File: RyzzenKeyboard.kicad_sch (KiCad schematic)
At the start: 30 parts, among them IC1 LD39100PU33RY, J1 TC2050, J2 Conn_01x16_Socket, J3 Conn_01x16_Socket, J4 USB_C_Receptacle_USB2.0_14P, U1 STM32F411CEUx, U37 W25Q32JVSS, Y1 25MHz

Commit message: [FIX](General) footprints
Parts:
- IC1: footprint SON95P300X300X90-7N-D -> LD39100PU33RY:SON95P300X300X90-7N-D
- renumbered D37 to D1, D1 to D2, J2 to J1, J3 to J2, J1 to J3, R4 to R1, R1 to R2, R11 to R3, R10 to R4, R2 to R5, R3 to R6, U37 to U1, U1 to U2
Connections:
- net VBUS: now also D1.2 (A); no longer D1.1 (K)
- net nCS0: no longer J1.8 (Pin_8), J2.8 (Pin_8)
- net nCS1: no longer J1.7 (Pin_7), J2.7 (Pin_7)
- net nCS2: now also J1.8 (Pin_8)
- net nCS3: now also J1.7 (Pin_7)
- net nCS4: now also J2.8 (Pin_8)
- net nCS5: now also J2.7 (Pin_7)
- net at J4.A4 (VBUS), J4.A9 (VBUS), J4.B4 (VBUS)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: now also D1.1 (K); no longer D1.2 (A)
- net Din renamed LED_Din
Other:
- sheet LEDs ports: added LED_5V, LED_DATA, LED_GND; removed Din, GND, Vcc
- moved on the sheet: D1

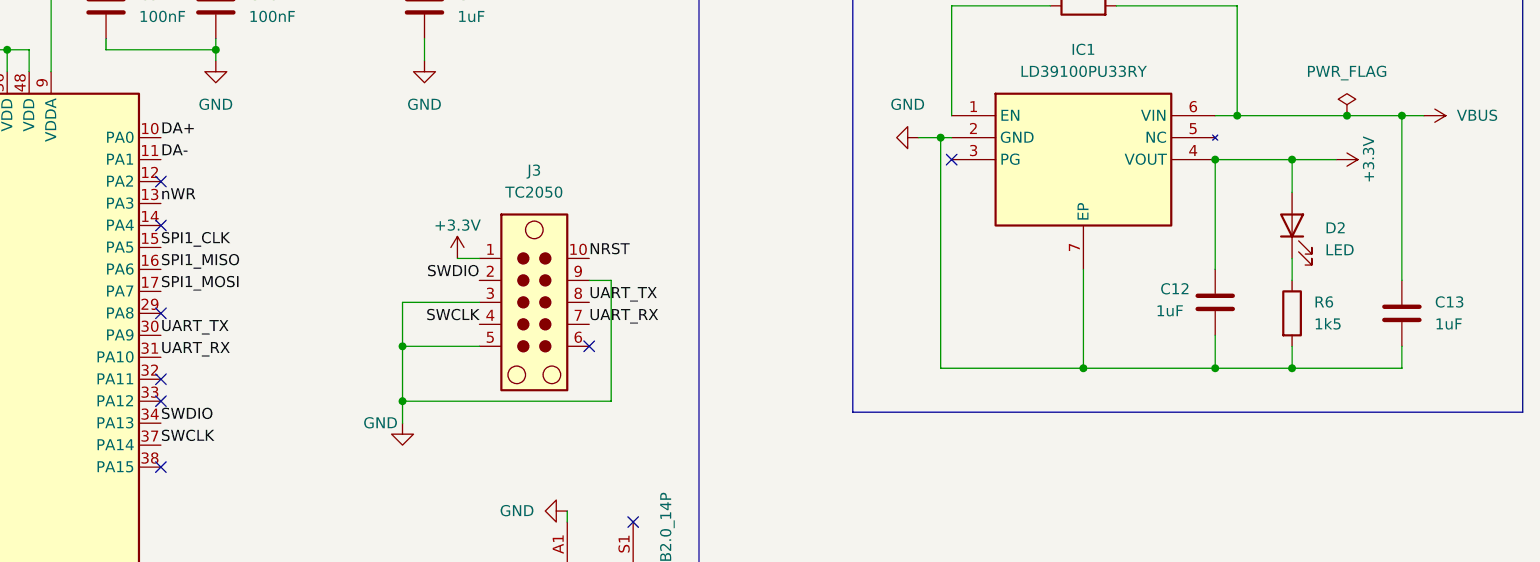
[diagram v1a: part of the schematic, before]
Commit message: [FIX](USB) main usb net labels
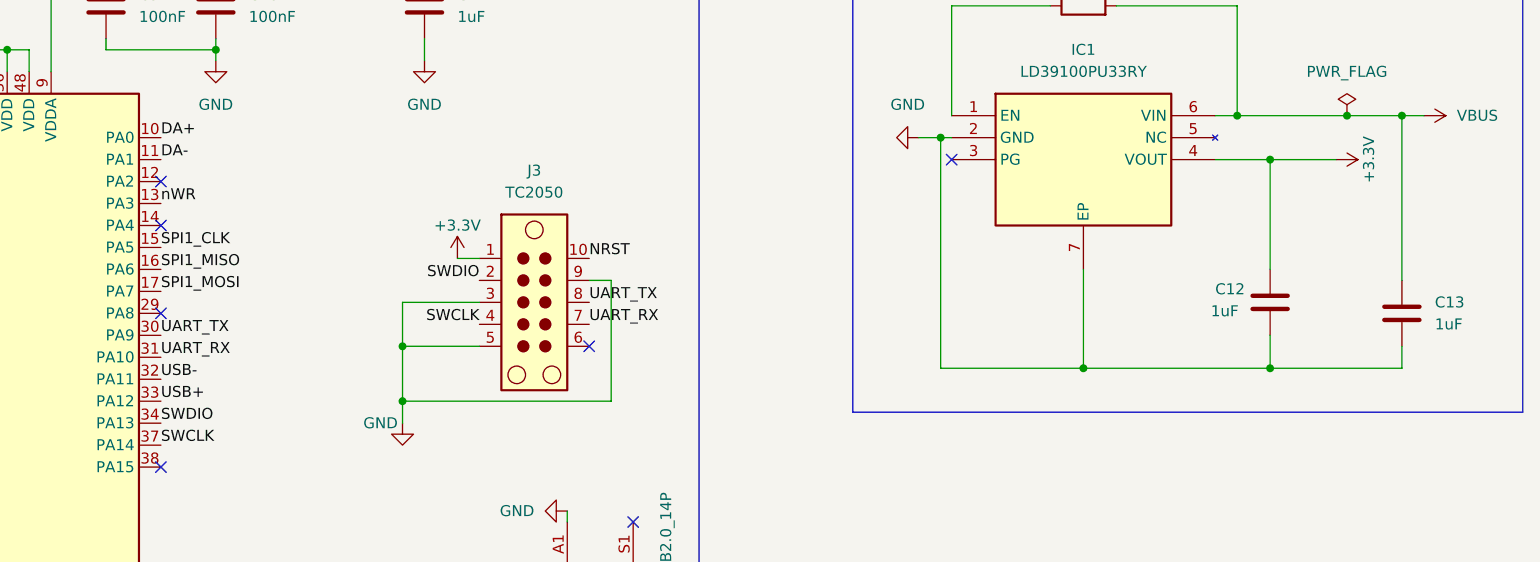
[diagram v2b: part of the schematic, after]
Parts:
- removed D2: LED, symbol Device:LED
- removed R6: 1k5, symbol Device:R
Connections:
- net USB+: now also U2.33 (PA12)
- net USB-: now also U2.32 (PA11)
- no-connect marks 13 -> 11
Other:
- moved on the sheet: C12
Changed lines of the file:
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@@
 	)
 	(junction
-		(at 247.65 80.01)
-		(diameter 0)
-		(color 0 0 0 0)
-	)
-	(junction
 		(at 35.56 43.18)
 		(diameter 0)
@@
 	)
 	(junction
-		(at 44.45 34.29)
+		(at 245.11 80.01)
 		(diameter 0)
 		(color 0 0 0 0)
 	)
 	(junction
-		(at 247.65 55.88)
+		(at 44.45 34.29)
 		(diameter 0)
 		(color 0 0 0 0)
@@
 	)
 	(junction
-		(at 238.76 80.01)
-		(diameter 0)
-		(color 0 0 0 0)
-	)
-	(junction
 		(at 58.42 91.44)
 		(diameter 0)
@@
 	)
 	(junction
-		(at 238.76 55.88)
+		(at 96.52 43.18)
 		(diameter 0)
 		(color 0 0 0 0)
 	)
 	(junction
-		(at 96.52 43.18)
+		(at 99.06 43.18)
 		(diameter 0)
 		(color 0 0 0 0)
 	)
 	(junction
-		(at 99.06 43.18)
+		(at 104.14 34.29)
 		(diameter 0)
 		(color 0 0 0 0)
 	)
 	(junction
-		(at 104.14 34.29)
+		(at 245.11 55.88)
 		(diameter 0)
 		(color 0 0 0 0)
@@
 	)
 	(no_connect
-		(at 116.84 83.82)
-	)
-	(no_connect
-		(at 116.84 81.28)
-	)
-	(no_connect
 		(at 166.37 77.47)
 	)
@@
 	(wire
 		(pts
-			(xy 223.52 80.01) (xy 238.76 80.01)
+			(xy 223.52 80.01) (xy 245.11 80.01)
 		)
 		(stroke
@@
 	(wire
 		(pts
-			(xy 247.65 55.88) (xy 252.73 55.88)
-		)
-		(stroke
-			(width 0)
-			(type default)
-		)
-	)
-	(wire
-		(pts
 			(xy 147.32 115.57) (xy 148.59 115.57)
 		)
@@
 	(wire
 		(pts
-			(xy 247.65 80.01) (xy 260.35 80.01)
+			(xy 62.23 76.2) (xy 62.23 83.82)
 		)
 		(stroke
@@
 	(wire
 		(pts
-			(xy 62.23 76.2) (xy 62.23 83.82)
+			(xy 110.49 34.29) (xy 116.84 34.29)
 		)
 		(stroke
@@
 	(wire
 		(pts
-			(xy 110.49 34.29) (xy 116.84 34.29)
+			(xy 147.32 30.48) (xy 147.32 34.29)
 		)
 		(stroke
@@
 	(wire
 		(pts
-			(xy 147.32 30.48) (xy 147.32 34.29)
+			(xy 101.6 43.18) (xy 101.6 45.72)
 		)
 		(stroke
@@
 	(wire
 		(pts
-			(xy 101.6 43.18) (xy 101.6 45.72)
+			(xy 31.75 123.19) (xy 27.94 123.19)
 		)
 		(stroke
@@
 	(wire
 		(pts
-			(xy 31.75 123.19) (xy 27.94 123.19)
+			(xy 245.11 80.01) (xy 260.35 80.01)
 		)
 		(stroke
@@
 	(wire
 		(pts
-			(xy 247.65 67.31) (xy 247.65 69.85)
-		)
-		(stroke
-			(width 0)
-			(type default)
-		)
-	)
-	(wire
-		(pts
 			(xy 148.59 123.19) (xy 147.32 123.19)
 		)
@@
 	(wire
 		(pts
-			(xy 238.76 80.01) (xy 247.65 80.01)
-		)
-		(stroke
-			(width 0)
-			(type default)
-		)
-	)
-	(wire
-		(pts
 			(xy 104.14 34.29) (xy 110.49 34.29)
 		)
@@
 	(wire
 		(pts
+			(xy 245.11 55.88) (xy 252.73 55.88)
+		)
+		(stroke
+			(width 0)
+			(type default)
+		)
+	)
+	(wire
+		(pts
 			(xy 146.05 120.65) (xy 147.32 120.65)
 		)
@@
 	(wire
 		(pts
-			(xy 238.76 68.58) (xy 238.76 55.88)
+			(xy 245.11 68.58) (xy 245.11 55.88)
 		)
 		(stroke
@@
 	(wire
 		(pts
-			(xy 247.65 55.88) (xy 247.65 59.69)
-		)
-		(stroke
-			(width 0)
-			(type default)
-		)
-	)
-	(wire
-		(pts
 			(xy 58.42 91.44) (xy 62.23 91.44)
 		)
@@
 	(wire
 		(pts
-			(xy 238.76 55.88) (xy 247.65 55.88)
-		)
-		(stroke
-			(width 0)
-			(type default)
-		)
-	)
-	(wire
-		(pts
-			(xy 247.65 77.47) (xy 247.65 80.01)
+			(xy 238.76 55.88) (xy 245.11 55.88)
 		)
 		(stroke
@@
 	(wire
 		(pts
-			(xy 238.76 76.2) (xy 238.76 80.01)
+			(xy 245.11 76.2) (xy 245.11 80.01)
 		)
 		(stroke
@@
 		)
 	)
+	(label "USB+"
+		(at 116.84 83.82 0)
+		(effects
+			(font
+				(size 1.27 1.27)
+			)
+			(justify left bottom)
+		)
+	)
 	(label "A3"
 		(at 81.28 106.68 180)
@@
 		)
 	)
+	(label "USB-"
+		(at 116.84 81.28 0)
+		(effects
+			(font
+				(size 1.27 1.27)
+			)
+			(justify left bottom)
+		)
+	)
 	(label "SPI1_MISO"
 		(at 116.84 68.58 0)
@@
 	(symbol
 		(lib_id "Device:C")
-		(at 238.76 72.39 0)
+		(at 245.11 72.39 0)
 		(unit 1)
 		(exclude_from_sim no)
@@
 		(dnp no)
 		(property "Reference" "C12"
-			(at 232.41 70.866 0)
+			(at 238.76 70.866 0)
 			(effects
 				(font
@@
 		)
 		(property "Value" "1uF"
-			(at 231.902 73.406 0)
+			(at 238.252 73.406 0)
 			(effects
 				(font
@@
 		)
 		(property "Footprint" ""
-			(at 239.7252 76.2 0)
+			(at 246.0752 76.2 0)
 			(effects
 				(font
@@
 		)
 		(property "Datasheet" "~"
-			(at 238.76 72.39 0)
+			(at 245.11 72.39 0)
 			(effects
 				(font
@@
 		)
 		(property "Description" "Unpolarized capacitor"
-			(at 238.76 72.39 0)
+			(at 245.11 72.39 0)
 			(effects
 				(font
@@
 	)
 	(symbol
-		(lib_id "Device:R")
-		(at 247.65 73.66 0)
-		(unit 1)
-		(exclude_from_sim no)
-		(in_bom yes)
-		(on_board yes)
-		(dnp no)
-		(fields_autoplaced yes)
-		(property "Reference" "R6"
-			(at 250.19 72.3899 0)
-			(effects
-				(font
-					(size 1.27 1.27)
-				)
-				(justify left)
-			)
-		)
-		(property "Value" "1k5"
-			(at 250.19 74.9299 0)
-			(effects
-				(font
-					(size 1.27 1.27)
-				)
-				(justify left)
-			)
-		)
-		(property "Footprint" ""
-			(at 245.872 73.66 90)
-			(effects
-				(font
-					(size 1.27 1.27)
-				)
-				(hide yes)
-			)
-		)
-		(property "Datasheet" "~"
-			(at 247.65 73.66 0)
-			(effects
-				(font
-					(size 1.27 1.27)
-				)
-				(hide yes)
-			)
-		)
-		(property "Description" "Resistor"
-			(at 247.65 73.66 0)
-			(effects
-				(font
-					(size 1.27 1.27)
-				)
-				(hide yes)
-			)
-		)
-		(pin "2"
-		)
-		(pin "1"
-		)
-		(instances
-			(project "RyzzenKeyboard"
-				(path "/5d44d704-6136-40a8-98a4-93f001ea8743"
-					(reference "R6")
-					(unit 1)
-				)
-			)
-		)
-	)
-	(symbol
 		(lib_id "power:GND")
 		(at 130.81 156.21 90)
@@
 	)
 	(symbol
-		(lib_id "Device:LED")
-		(at 247.65 63.5 90)
-		(unit 1)
-		(exclude_from_sim no)
-		(in_bom yes)
-		(on_board yes)
-		(dnp no)
-		(fields_autoplaced yes)
-		(property "Reference" "D2"
-			(at 251.46 63.8174 90)
-			(effects
-				(font
-					(size 1.27 1.27)
-				)
-				(justify right)
-			)
-		)
-		(property "Value" "LED"
-			(at 251.46 66.3574 90)
-			(effects
-				(font
-					(size 1.27 1.27)
-				)
-				(justify right)
-			)
-		)
-		(property "Footprint" ""
-			(at 247.65 63.5 0)
-			(effects
-				(font
-					(size 1.27 1.27)
-				)
-				(hide yes)
-			)
-		)
-		(property "Datasheet" "~"
-			(at 247.65 63.5 0)
-			(effects
-				(font
-					(size 1.27 1.27)
-				)
-				(hide yes)
-			)
-		)
-		(property "Description" "Light emitting diode"
-			(at 247.65 63.5 0)
-			(effects
-				(font
-					(size 1.27 1.27)
-				)
-				(hide yes)
-			)
-		)
-		(property "Sim.Pins" "1=K 2=A"
-			(at 247.65 63.5 0)
-			(effects
-				(font
-					(size 1.27 1.27)
-				)
-				(hide yes)
-			)
-		)
-		(pin "2"
-		)
-		(pin "1"
-		)
-		(instances
-			(project "RyzzenKeyboard"
-				(path "/5d44d704-6136-40a8-98a4-93f001ea8743"
-					(reference "D2")
-					(unit 1)
-				)
-			)
-		)
-	)
-	(symbol
 		(lib_id "Memory_Flash:W25Q32JVSS")
 		(at 41.91 120.65 0)
@@
 			(project "RyzzenKeyboard"
 				(path "/5d44d704-6136-40a8-98a4-93f001ea8743"
-					(page "106")
+					(page "120")
 				)
 			)
@@
 			(project "RyzzenKeyboard"
 				(path "/5d44d704-6136-40a8-98a4-93f001ea8743"
-					(page "108")
+					(page "5")
 				)
 			)

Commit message: [ADD](General) added all footprints expect leds
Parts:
- C1, C10, C11, C12, C13, C2, C3, C4, C5, C6, C7, C8, C9: footprint (none) -> Capacitor_SMD:C_0603_1608Metric_Pad1.08x0.95mm_HandSolder
- J1, J2: footprint (none) -> Connector_JST:JST_XH_S16B-XH-A_1x16_P2.50mm_Horizontal
- R1, R2, R3, R4, R5: footprint (none) -> Resistor_SMD:R_0603_1608Metric_Pad0.98x0.95mm_HandSolder
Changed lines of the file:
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@@
 			)
 		)
-		(property "Footprint" ""
+		(property "Footprint" "Capacitor_SMD:C_0603_1608Metric_Pad1.08x0.95mm_HandSolder"
 			(at 49.53 54.3052 0)
 			(effects
@@
 			)
 		)
-		(property "Footprint" ""
+		(property "Footprint" "Resistor_SMD:R_0603_1608Metric_Pad0.98x0.95mm_HandSolder"
 			(at 223.52 39.878 90)
 			(effects
@@
 			)
 		)
-		(property "Footprint" ""
+		(property "Footprint" "Capacitor_SMD:C_0603_1608Metric_Pad1.08x0.95mm_HandSolder"
 			(at 58.1152 41.91 0)
 			(effects
@@
 			)
 		)
-		(property "Footprint" ""
+		(property "Footprint" "Capacitor_SMD:C_0603_1608Metric_Pad1.08x0.95mm_HandSolder"
 			(at 111.4552 41.91 0)
 			(effects
@@
 			)
 		)
-		(property "Footprint" ""
+		(property "Footprint" "Capacitor_SMD:C_0603_1608Metric_Pad1.08x0.95mm_HandSolder"
 			(at 32.7152 41.91 0)
 			(effects
@@
 			)
 		)
-		(property "Footprint" ""
+		(property "Footprint" "Capacitor_SMD:C_0603_1608Metric_Pad1.08x0.95mm_HandSolder"
 			(at 47.9552 91.44 0)
 			(effects
@@
 			)
 		)
-		(property "Footprint" ""
+		(property "Footprint" "Capacitor_SMD:C_0603_1608Metric_Pad1.08x0.95mm_HandSolder"
 			(at 70.8152 41.91 0)
 			(effects
@@
 			)
 		)
-		(property "Footprint" ""
+		(property "Footprint" "Capacitor_SMD:C_0603_1608Metric_Pad1.08x0.95mm_HandSolder"
 			(at 246.0752 76.2 0)
 			(effects
@@
 			)
 		)
-		(property "Footprint" ""
+		(property "Footprint" "Capacitor_SMD:C_0603_1608Metric_Pad1.08x0.95mm_HandSolder"
 			(at 148.2852 41.91 0)
 			(effects
@@
 			)
 		)
-		(property "Footprint" ""
+		(property "Footprint" "Capacitor_SMD:C_0603_1608Metric_Pad1.08x0.95mm_HandSolder"
 			(at 45.4152 41.91 0)
 			(effects
@@
 			)
 		)
-		(property "Footprint" ""
+		(property "Footprint" "Resistor_SMD:R_0603_1608Metric_Pad0.98x0.95mm_HandSolder"
 			(at 29.718 130.81 90)
 			(effects
@@
 			)
 		)
-		(property "Footprint" ""
+		(property "Footprint" "Capacitor_SMD:C_0603_1608Metric_Pad1.08x0.95mm_HandSolder"
 			(at 124.1552 41.91 0)
 			(effects
@@
 			)
 		)
-		(property "Footprint" ""
+		(property "Footprint" "Resistor_SMD:R_0603_1608Metric_Pad0.98x0.95mm_HandSolder"
 			(at 143.51 132.588 90)
 			(effects
@@
 			)
 		)
-		(property "Footprint" ""
+		(property "Footprint" "Capacitor_SMD:C_0603_1608Metric_Pad1.08x0.95mm_HandSolder"
 			(at 83.5152 41.91 0)
 			(effects
@@
 			)
 		)
-		(property "Footprint" ""
+		(property "Footprint" "Capacitor_SMD:C_0603_1608Metric_Pad1.08x0.95mm_HandSolder"
 			(at 63.1952 91.44 0)
 			(effects
@@
 			)
 		)
-		(property "Footprint" ""
+		(property "Footprint" "Capacitor_SMD:C_0603_1608Metric_Pad1.08x0.95mm_HandSolder"
 			(at 261.3152 77.47 0)
 			(effects
@@
 			)
 		)
-		(property "Footprint" ""
+		(property "Footprint" "Resistor_SMD:R_0603_1608Metric_Pad0.98x0.95mm_HandSolder"
 			(at 67.31 60.198 90)
 			(effects
@@
 			)
 		)
-		(property "Footprint" ""
+		(property "Footprint" "Resistor_SMD:R_0603_1608Metric_Pad0.98x0.95mm_HandSolder"
 			(at 143.51 130.048 90)
 			(effects
@@
 			)
 		)
-		(property "Footprint" ""
+		(property "Footprint" "Connector_JST:JST_XH_S16B-XH-A_1x16_P2.50mm_Horizontal"
 			(at 149.86 176.53 0)
 			(effects
@@
 			)
 		)
-		(property "Footprint" ""
+		(property "Footprint" "Connector_JST:JST_XH_S16B-XH-A_1x16_P2.50mm_Horizontal"
 			(at 125.73 176.53 0)
 			(effects

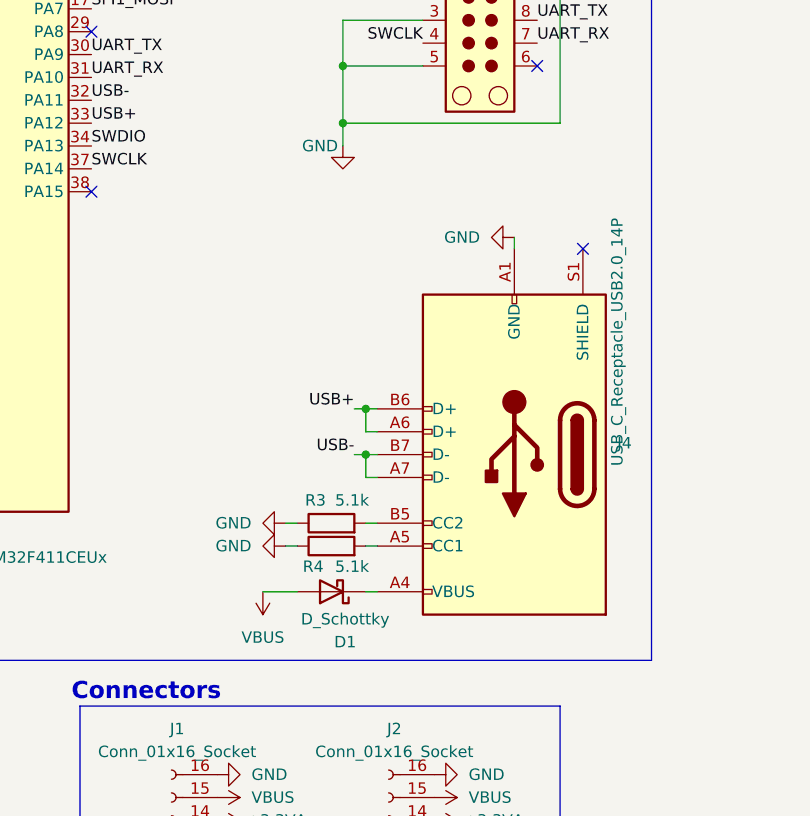
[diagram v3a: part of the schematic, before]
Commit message: [ADD](General) added all footprints
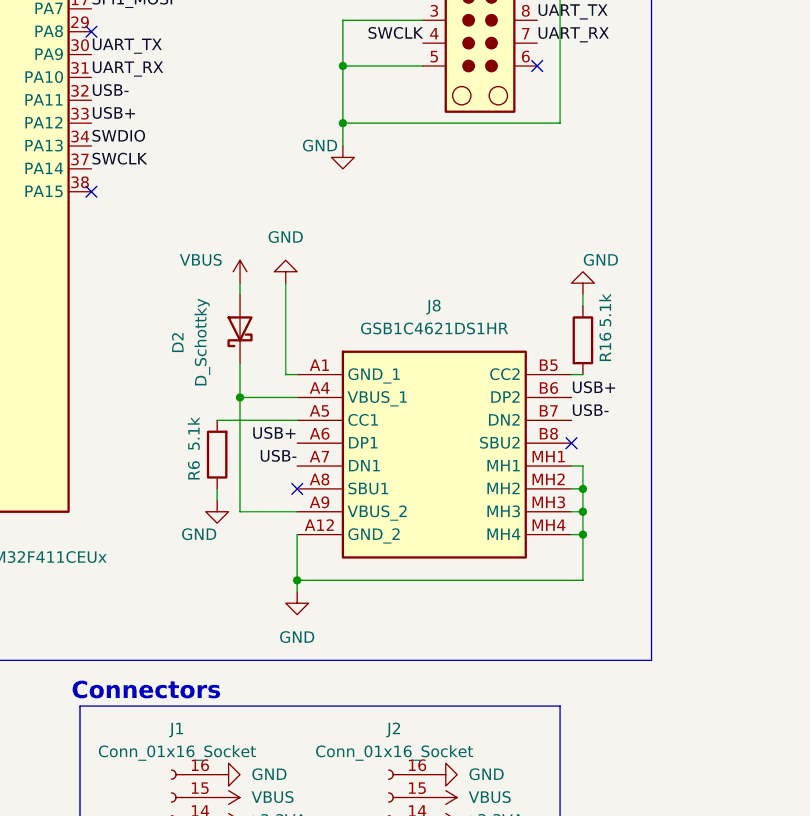
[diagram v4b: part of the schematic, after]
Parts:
- removed D1: D_Schottky, symbol Device:D_Schottky
- removed J4: USB_C_Receptacle_USB2.0_14P, symbol Connector:USB_C_Receptacle_USB2.0_14P
- removed R3, R4: 5.1k, Resistor_SMD:R_0603_1608Metric_Pad0.98x0.95mm_HandSolder, symbol Device:R
- added D2: D_Schottky, CUHS20S30:CUHS20S40H3F, symbol Device:D_Schottky
- added J8: GSB1C4621DS1HR, GSB1C4621DS1HR:GSB1C4621DS1HR, symbol GSB1C4621DS1HR:GSB1C4621DS1HR
- added R16, R6: 5.1k, Resistor_SMD:R_0603_1608Metric_Pad0.98x0.95mm_HandSolder, symbol Device:R
- FB1: footprint (none) -> BLM21PG121SN1D:BLM21AG102BH1J
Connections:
- net GND: now also J8.A1 (GND_1), J8.A12 (GND_2), J8.MH1, J8.MH2, J8.MH3, J8.MH4, R16.1, R6.1
- net USB+: now also J8.A6 (DP1), J8.B6 (DP2)
- net USB-: now also J8.A7 (DN1), J8.B7 (DN2)
- net VBUS: now also D2.2 (A)
- new net: J8.B5 (CC2), R16.2
- new net: D2.1 (K), J8.A4 (VBUS_1), J8.A9 (VBUS_2)
- new net: J8.A5 (CC1), R6.2
- no-connect marks 11 -> 12
